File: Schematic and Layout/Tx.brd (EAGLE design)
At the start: 76.2 x 63.5 mm, 31 parts

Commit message: Add files via upload
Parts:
- U$1: value LED_1206 -> LED_12V
- U$10, U$9: value CAP_POL -> 10uF
- U$11: value LED_1206 -> LED_5V
- U$12, U$15, U$21, U$23, U$27, U$4: value RES -> 1K
- U$16: value RES -> 5.1
- U$17, U$18: value CAP -> 100nF
- U$19: value LED_1206 -> LED_GAS
- U$2: value CAP -> 470u
- U$20: value DIODE_Z_1005 -> 15V_Z
- U$22: value RES -> 100K
- U$24: value CAP -> 1uF
- U$25, U$26: value RES -> ?
- U$3: value RES -> 330
- U$5: value DIODE_1206 -> DIODE
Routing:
- net N$14: track 64.3 -> 65.1 mm

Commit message: Add files via upload
I added an output LED on the receiver side and put some silkscreen on the bottom with our first names. 
I also added "RESET" next to the button on the silkscreen for the rx.
Input capacitance decreased to 10uF. Too expensive to get 470uF.
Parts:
- U$2: value 470u -> 10uF
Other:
- board text added: "Alec Arsalan Kam Noah"
- board text added: "TRANCEIVER - TX CAPSTONE SPRING 2017"
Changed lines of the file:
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@@
 <text x="58.928" y="5.969" size="1.778" layer="21">ESP8266</text>
 <text x="45.72" y="11.176" size="1.778" layer="21" rot="R90">GAS SENSOR TX</text>
+<text x="71.882" y="28.448" size="1.778" layer="22" rot="MR270">TRANCEIVER - TX
+CAPSTONE SPRING 2017</text>
+<text x="66.294" y="9.398" size="1.778" layer="22" rot="MR270">Alec
+Arsalan
+Kam
+Noah</text>
 </plain>
 <attributes>
@@
 <attribute name="VALUE" x="42.647" y="0.635" size="1.27" layer="27"/>
 </element>
-<element name="U$2" library="Gas_Sensor_Lib_v1" package="C1206" value="470u" x="18.796" y="9.144" smashed="yes" rot="R90">
+<element name="U$2" library="Gas_Sensor_Lib_v1" package="C1206" value="10uF" x="18.796" y="9.144" smashed="yes" rot="R90">
 <attribute name="NAME" x="16.002" y="7.493" size="1.27" layer="25" rot="R90"/>
 <attribute name="VALUE" x="14.478" y="7.366" size="1.27" layer="27" rot="R90"/>
@@
 </board>
 </drawing>
+<compatibility>
+<note version="6.3" minversion="6.2.2" severity="warning">
+Since Version 6.2.2 text objects can contain more than one line,
+which will not be processed correctly with this version.
+</note>
+</compatibility>
 </eagle>

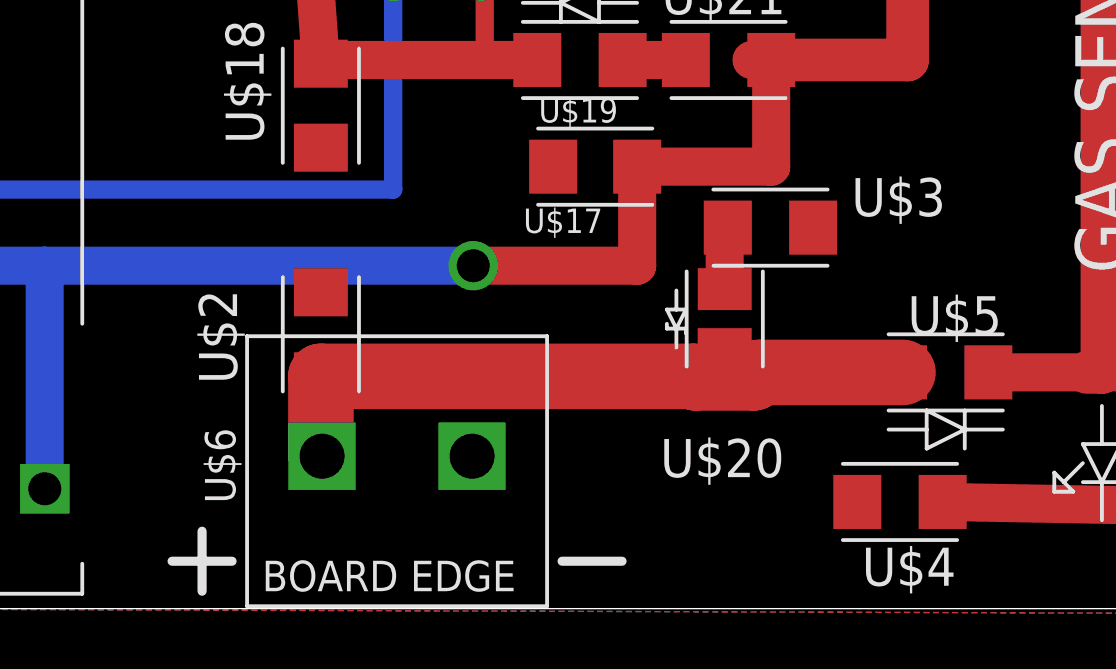
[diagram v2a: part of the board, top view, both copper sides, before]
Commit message: Fixed major error on tx board. Cap overlapped connector
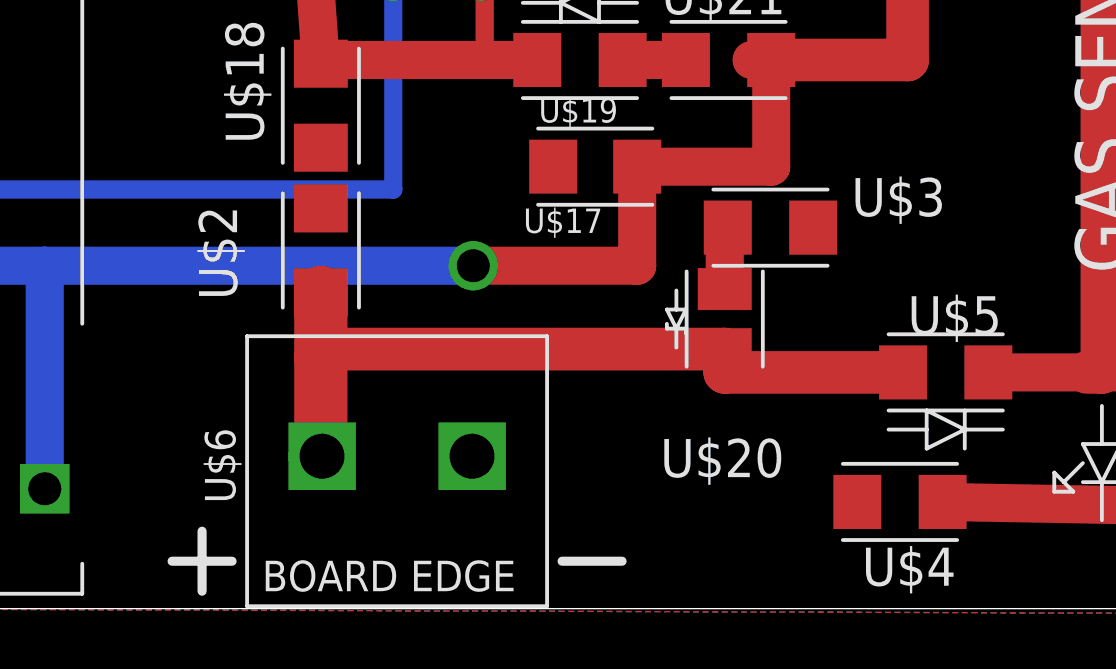
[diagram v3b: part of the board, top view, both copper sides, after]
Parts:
- moved U$2 2.79 mm to (18.8, 11.9)
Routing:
- net 12V_IN: track 29.4 -> 26.0 mm
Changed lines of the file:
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@@
 <text x="58.928" y="5.969" size="1.778" layer="21">ESP8266</text>
 <text x="45.72" y="11.176" size="1.778" layer="21" rot="R90">GAS SENSOR TX</text>
-<text x="71.882" y="28.448" size="1.778" layer="22" rot="MR270">TRANCEIVER - TX
+<text x="71.882" y="30.48" size="1.778" layer="22" rot="MR270">TRANCEIVER - TX
 CAPSTONE SPRING 2017</text>
-<text x="66.294" y="9.398" size="1.778" layer="22" rot="MR270">Alec
+<text x="66.294" y="11.176" size="1.778" layer="22" rot="MR270">Alec
 Arsalan
 Kam
@@
 <attribute name="VALUE" x="42.647" y="0.635" size="1.27" layer="27"/>
 </element>
-<element name="U$2" library="Gas_Sensor_Lib_v1" package="C1206" value="10uF" x="18.796" y="9.144" smashed="yes" rot="R90">
-<attribute name="NAME" x="16.002" y="7.493" size="1.27" layer="25" rot="R90"/>
-<attribute name="VALUE" x="14.478" y="7.366" size="1.27" layer="27" rot="R90"/>
+<element name="U$2" library="Gas_Sensor_Lib_v1" package="C1206" value="10uF" x="18.796" y="11.938" smashed="yes" rot="R90">
+<attribute name="NAME" x="16.002" y="10.287" size="1.27" layer="25" rot="R90"/>
+<attribute name="VALUE" x="14.478" y="10.16" size="1.27" layer="27" rot="R90"/>
 </element>
 <element name="U$3" library="Gas_Sensor_Lib_v1" package="R1206" value="330" x="33.782" y="12.7" smashed="yes" rot="R180">
@@
 <contactref element="U$20" pad="2"/>
 <contactref element="U$5" pad="1"/>
-<wire x1="18.836" y1="5.08" x2="18.796" y2="5.08" width="2.1844" layer="1"/>
-<wire x1="18.796" y1="7.744" x2="18.796" y2="5.08" width="2.1844" layer="1"/>
-<wire x1="38.202" y1="7.874" x2="33.40613125" y2="7.874" width="2.1844" layer="1"/>
-<wire x1="33.40613125" y1="7.874" x2="33.22353125" y2="7.6914" width="2.1844" layer="1"/>
-<wire x1="33.22353125" y1="7.6914" x2="31.29246875" y2="7.6914" width="2.1844" layer="1"/>
-<wire x1="31.29246875" y1="7.6914" x2="31.23986875" y2="7.744" width="2.1844" layer="1"/>
-<wire x1="31.23986875" y1="7.744" x2="18.796" y2="7.744" width="2.1844" layer="1"/>
-<wire x1="32.258" y1="7.62" x2="38.202" y2="7.62" width="0.3048" layer="1"/>
-<wire x1="38.202" y1="7.62" x2="38.202" y2="7.874" width="0.3048" layer="1"/>
-<wire x1="32.258" y1="8.652" x2="32.258" y2="7.62" width="0.3048" layer="1"/>
+<wire x1="18.796" y1="5.08" x2="18.836" y2="5.08" width="2.1844" layer="1"/>
+<wire x1="18.836" y1="5.08" x2="18.796" y2="5.08" width="1.778" layer="1"/>
+<wire x1="18.796" y1="8.382" x2="18.796" y2="5.08" width="1.778" layer="1"/>
+<wire x1="18.796" y1="8.382" x2="18.796" y2="10.538" width="1.778" layer="1"/>
+<wire x1="38.202" y1="7.874" x2="32.258" y2="7.874" width="1.4224" layer="1"/>
+<wire x1="32.258" y1="7.874" x2="32.258" y2="8.652" width="1.4224" layer="1"/>
+<wire x1="32.258" y1="8.652" x2="18.796" y2="8.652" width="1.4224" layer="1"/>
+<wire x1="18.796" y1="8.652" x2="18.796" y2="8.382" width="1.4224" layer="1"/>
 </signal>
 <signal name="12V">

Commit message: Minor changes
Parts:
- moved U$3 3.09 mm to (36.8, 12.2)
- moved U$8 0.25 mm to (46.1, 53.1)
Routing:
- net 5V: track 156.0 -> 151.2 mm
- net N$5: track 2.06 -> 4.69 mm
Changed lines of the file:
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@@
 <text x="58.928" y="5.969" size="1.778" layer="21">ESP8266</text>
 <text x="45.72" y="11.176" size="1.778" layer="21" rot="R90">GAS SENSOR TX</text>
-<text x="71.882" y="30.48" size="1.778" layer="22" rot="MR270">TRANCEIVER - TX
+<text x="70.358" y="38.608" size="1.778" layer="22" rot="MR270">TRANCEIVER - TX
 CAPSTONE SPRING 2017</text>
-<text x="66.294" y="11.176" size="1.778" layer="22" rot="MR270">Alec
+<text x="65.024" y="19.558" size="1.778" layer="22" rot="MR270">Alec
 Arsalan
 Kam
@@
 <attribute name="VALUE" x="14.478" y="10.16" size="1.27" layer="27" rot="R90"/>
 </element>
-<element name="U$3" library="Gas_Sensor_Lib_v1" package="R1206" value="330" x="33.782" y="12.7" smashed="yes" rot="R180">
-<attribute name="NAME" x="39.624" y="14.351" size="1.27" layer="25" rot="R180"/>
-<attribute name="VALUE" x="39.37" y="12.7" size="1.27" layer="27" rot="R180"/>
+<element name="U$3" library="Gas_Sensor_Lib_v1" package="R1206" value="330" x="36.83" y="12.192" smashed="yes" rot="R180">
+<attribute name="NAME" x="38.862" y="15.113" size="1.27" layer="25" rot="R180"/>
+<attribute name="VALUE" x="42.164" y="14.478" size="1.27" layer="27" rot="R180"/>
 </element>
 <element name="U$4" library="Gas_Sensor_Lib_v1" package="R1206" value="1K" x="38.1" y="3.556" smashed="yes">
@@
 <attribute name="VALUE" x="36.957" y="22.987" size="1.27" layer="27" rot="R90"/>
 </element>
-<element name="U$8" library="Gas_Sensor_Lib_v1" package="SOT223" value="5V_REG" x="45.847" y="53.086" smashed="yes" rot="R270">
-<attribute name="NAME" x="47.217" y="49.2242" size="1.27" layer="25" rot="R180"/>
-<attribute name="VALUE" x="52.1262" y="55.876" size="1.27" layer="27" rot="R270"/>
+<element name="U$8" library="Gas_Sensor_Lib_v1" package="SOT223" value="5V_REG" x="46.101" y="53.086" smashed="yes" rot="R270">
+<attribute name="NAME" x="47.471" y="49.2242" size="1.27" layer="25" rot="R180"/>
+<attribute name="VALUE" x="52.3802" y="55.876" size="1.27" layer="27" rot="R270"/>
 </element>
 <element name="U$9" library="Gas_Sensor_Lib_v1" package="153CLV-0405" value="10uF" x="43.561" y="59.563" smashed="yes">
@@
 <wire x1="46.736" y1="6.604" x2="46.736" y2="6.273" width="1.27" layer="1"/>
 <wire x1="42.8752" y1="46.5728" x2="42.966" y2="45.339" width="1.4224" layer="1"/>
-<wire x1="42.8752" y1="46.5728" x2="42.7482" y2="50.7746" width="1.4224" layer="1"/>
+<wire x1="42.8752" y1="46.5728" x2="43.0022" y2="50.7746" width="1.4224" layer="1"/>
 <wire x1="42.966" y1="45.339" x2="42.966" y2="39.497" width="1.4224" layer="1"/>
 <wire x1="42.966" y1="39.497" x2="44.831" y2="39.497" width="1.4224" layer="1"/>
@@
 <contactref element="U$13" pad="8"/>
 <wire x1="35.347" y1="45.58" x2="32.537" y2="48.39" width="2.54" layer="1"/>
-<wire x1="37.907" y1="51.75" x2="33.927" y2="51.75" width="2.54" layer="1"/>
+<wire x1="33.927" y1="51.75" x2="37.907" y2="51.75" width="2.54" layer="1"/>
 <wire x1="35.347" y1="57.92" x2="32.537" y2="55.11" width="2.54" layer="1"/>
-<wire x1="32.537" y1="55.11" x2="30.505" y2="52.378" width="2.54" layer="1"/>
-<wire x1="30.505" y1="52.378" x2="33.927" y2="51.75" width="2.54" layer="1"/>
-<wire x1="32.537" y1="48.39" x2="30.505" y2="49.598" width="2.54" layer="1"/>
-<wire x1="30.505" y1="49.598" x2="33.927" y2="51.75" width="2.54" layer="1"/>
 <wire x1="33.807" y1="18.288" x2="33.15" y2="18.288" width="1.27" layer="1"/>
 <wire x1="33.807" y1="18.288" x2="33.807" y2="14.732" width="1.27" layer="1"/>
@@
 <wire x1="4.592" y1="11.43" x2="9.592" y2="11.43" width="1.27" layer="16"/>
 <contactref element="U$31" pad="P$1"/>
-<wire x1="46.061" y1="59.563" x2="48.184" y2="59.563" width="1.4224" layer="1"/>
-<wire x1="48.184" y1="59.563" x2="48.946" y2="53.086" width="1.4224" layer="1"/>
-<wire x1="37.907" y1="51.75" x2="42.7482" y2="53.086" width="1.4224" layer="1"/>
-<wire x1="42.7482" y1="53.086" x2="48.946" y2="53.086" width="1.4224" layer="1"/>
-<wire x1="48.946" y1="53.086" x2="59.436" y2="52.959" width="3.81" layer="1"/>
+<wire x1="49.2" y1="53.086" x2="43.0022" y2="53.086" width="1.4224" layer="1"/>
 <wire x1="59.436" y1="52.959" x2="62.738" y2="55.753" width="3.81" layer="1" curve="90"/>
 <wire x1="38.354" y1="30.836" x2="38.354" y2="18.288" width="1.4224" layer="1"/>
@@
 <wire x1="38.354" y1="30.836" x2="38.354" y2="28.829" width="0.6096" layer="1"/>
 <wire x1="38.354" y1="28.829" x2="33.334" y2="28.829" width="0.6096" layer="1"/>
+<wire x1="49.2" y1="53.086" x2="59.436" y2="53.086" width="1.778" layer="1"/>
+<wire x1="59.436" y1="53.086" x2="59.436" y2="52.959" width="1.778" layer="1"/>
+<wire x1="43.0022" y1="53.086" x2="40.386" y2="53.086" width="1.4224" layer="1"/>
+<wire x1="40.386" y1="53.086" x2="37.907" y2="51.75" width="1.4224" layer="1"/>
+<wire x1="32.537" y1="55.11" x2="33.927" y2="51.75" width="2.1844" layer="1"/>
+<wire x1="32.537" y1="48.39" x2="33.927" y2="51.75" width="2.1844" layer="1"/>
+<wire x1="46.061" y1="59.563" x2="49.2" y2="59.563" width="2.1844" layer="1"/>
+<wire x1="49.2" y1="59.563" x2="49.2" y2="53.086" width="2.1844" layer="1"/>
 </signal>
 <signal name="N$3">
@@
 <contactref element="U$16" pad="2"/>
 <contactref element="U$13" pad="11"/>
-<wire x1="20.447" y1="51.75" x2="24.427" y2="51.75" width="2.54" layer="1"/>
 <wire x1="13.97" y1="51.156" x2="16.535" y2="51.75" width="1.4224" layer="1"/>
 <wire x1="16.535" y1="51.75" x2="20.447" y2="51.75" width="1.4224" layer="1"/>
+<wire x1="20.447" y1="51.75" x2="24.427" y2="51.75" width="2.1844" layer="1"/>
 </signal>
 <signal name="N$6">
@@
 <contactref element="U$20" pad="1"/>
 <contactref element="U$3" pad="2"/>
-<wire x1="32.36" y1="12.7" x2="32.258" y2="12.192" width="1.27" layer="1"/>
+<wire x1="35.408" y1="12.192" x2="32.258" y2="12.192" width="1.27" layer="1"/>
 <wire x1="32.258" y1="12.192" x2="32.258" y2="10.652" width="1.27" layer="1"/>
 </signal>
@@
 </signal>
 </signals>
+<errors>
+</errors>
 </board>
 </drawing>

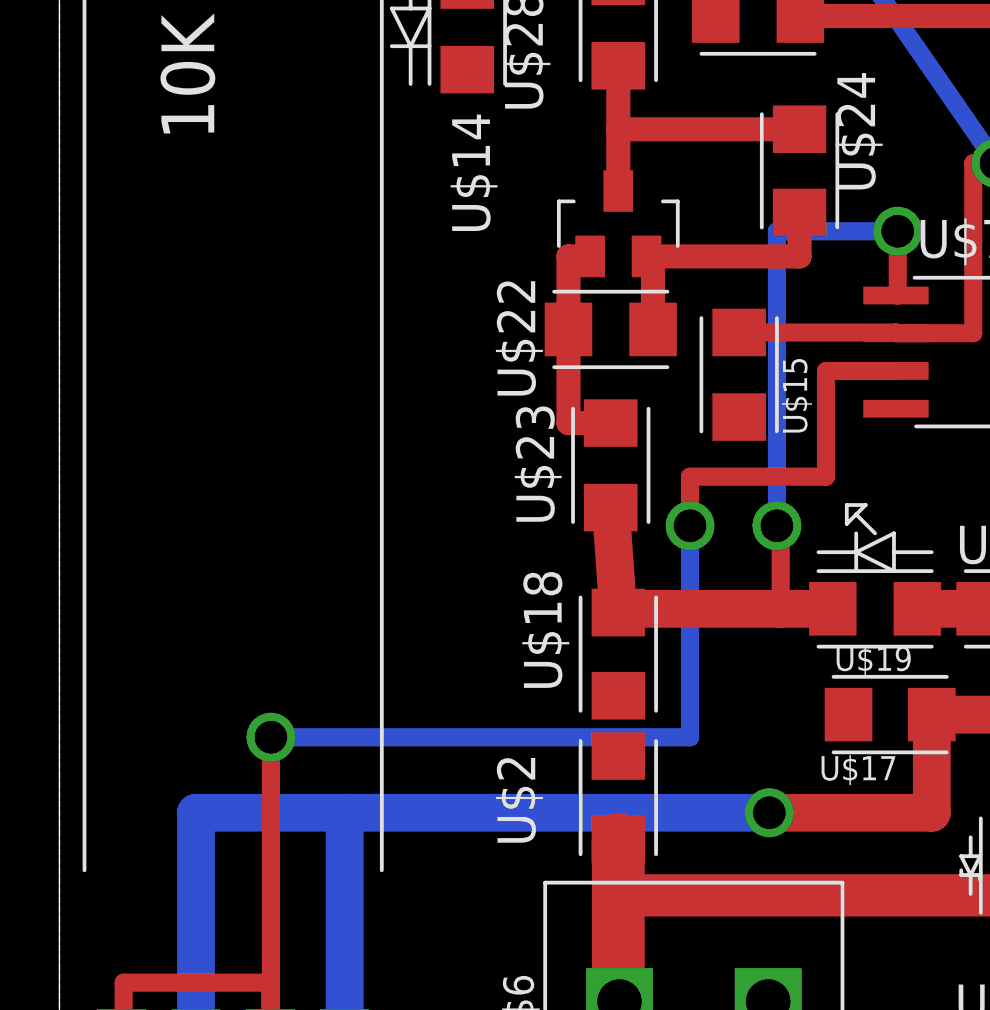
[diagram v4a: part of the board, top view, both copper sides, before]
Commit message: Major error fixed, was missing 5V on PNP
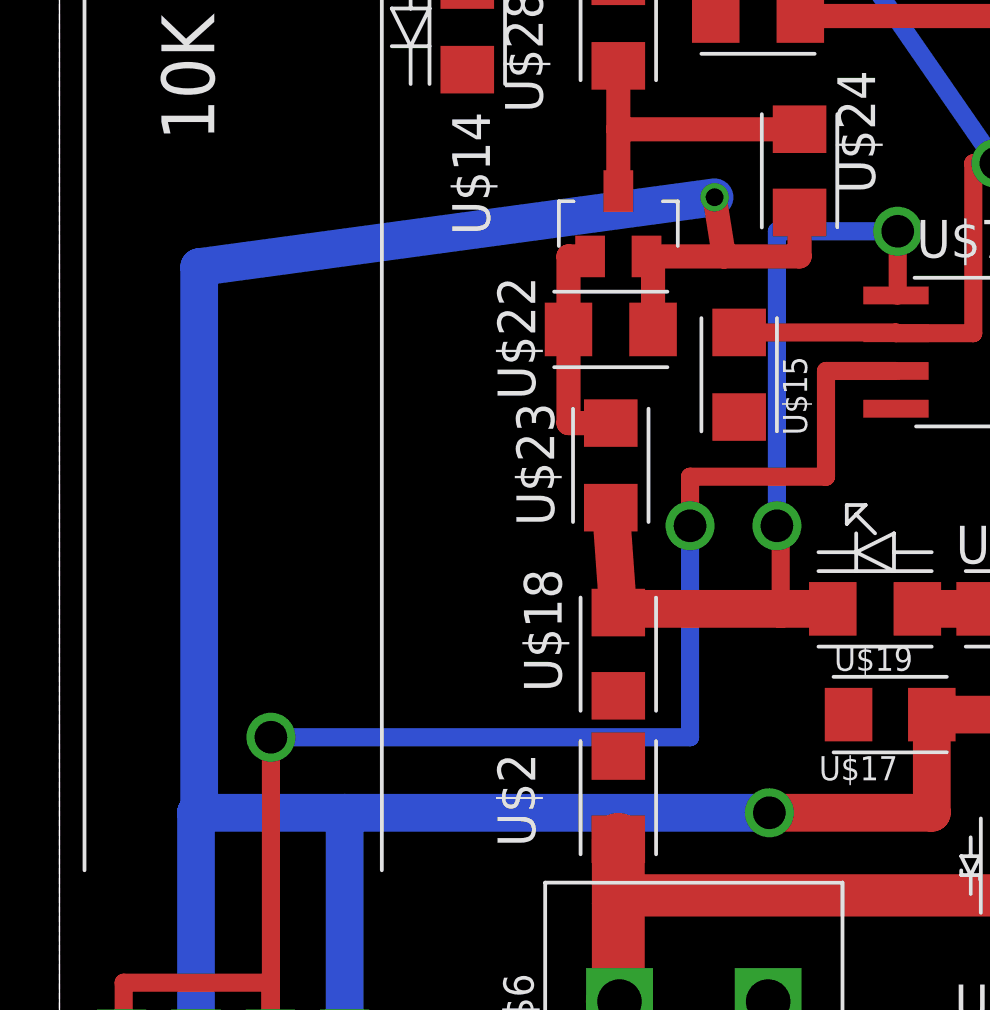
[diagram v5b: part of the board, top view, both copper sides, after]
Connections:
- removed net N$10: U$14.2, U$22.1, U$24.1
- net 5V: now also U$14.2, U$22.1, U$24.1
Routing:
- net 5V: track 151.2 -> 198.5 mm, vias 2 -> 3
- net N$10: track 9.30 -> 0.00 mm
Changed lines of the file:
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@@
 <setting verticaltext="up"/>
 </settings>
-<grid distance="0.01" unitdist="inch" unit="inch" style="dots" multiple="1" display="yes" altdistance="0.025" altunitdist="inch" altunit="inch"/>
+<grid distance="0.0025" unitdist="inch" unit="inch" style="dots" multiple="1" display="yes" altdistance="0.025" altunitdist="inch" altunit="inch"/>
 <layers>
 <layer number="1" name="Top" color="4" fill="1" visible="yes" active="yes"/>
@@
 <wire x1="46.061" y1="59.563" x2="49.2" y2="59.563" width="2.1844" layer="1"/>
 <wire x1="49.2" y1="59.563" x2="49.2" y2="53.086" width="2.1844" layer="1"/>
+<contactref element="U$22" pad="1"/>
+<contactref element="U$14" pad="2"/>
+<contactref element="U$24" pad="1"/>
+<wire x1="19.746" y1="30.142" x2="19.964" y2="30.142" width="0.8128" layer="1"/>
+<wire x1="19.964" y1="30.142" x2="19.964" y2="27.686" width="0.8128" layer="1"/>
+<wire x1="24.892" y1="31.62" x2="24.892" y2="30.142" width="0.8128" layer="1"/>
+<wire x1="22.352" y1="30.142" x2="24.892" y2="30.142" width="0.8128" layer="1"/>
+<wire x1="22.352" y1="30.142" x2="19.746" y2="30.142" width="0.8128" layer="1"/>
+<wire x1="4.592" y1="11.43" x2="4.699" y2="11.43" width="1.27" layer="16"/>
+<wire x1="4.699" y1="11.43" x2="4.699" y2="29.7815" width="1.27" layer="16"/>
+<wire x1="4.699" y1="29.7815" x2="22.0345" y2="32.131" width="1.27" layer="16"/>
+<via x="22.0345" y="32.131" extent="1-16" drill="0.6" shape="square"/>
+<wire x1="22.0345" y1="32.131" x2="22.352" y2="30.142" width="0.8128" layer="1"/>
 </signal>
 <signal name="N$3">
@@
 <wire x1="17.12" y1="24.536" x2="18.542" y2="24.536" width="0.8128" layer="1"/>
 </signal>
-<signal name="N$10">
-<contactref element="U$22" pad="1"/>
-<contactref element="U$14" pad="2"/>
-<contactref element="U$24" pad="1"/>
-<wire x1="19.746" y1="30.142" x2="19.964" y2="30.142" width="0.8128" layer="1"/>
-<wire x1="19.964" y1="30.142" x2="19.964" y2="27.686" width="0.8128" layer="1"/>
-<wire x1="24.892" y1="31.62" x2="24.892" y2="30.142" width="0.8128" layer="1"/>
-<wire x1="24.892" y1="30.142" x2="19.746" y2="30.142" width="0.8128" layer="1"/>
-</signal>
 <signal name="N$11">
